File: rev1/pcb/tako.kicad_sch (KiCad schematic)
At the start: 118 parts, among them J1 MJ-4PP-9, J101 MJ-4PP-9, SW1 EC_SW, SW10 EC_SW, SW101 EC_SW, SW102 EC_SW, SW103 EC_SW, SW104 EC_SW, SW105 EC_SW, SW106 EC_SW, SW107 EC_SW, SW108 EC_SW, SW109 EC_SW, SW11 EC_SW, SW110 EC_SW, SW111 EC_SW, SW112 EC_SW, SW113 EC_SW, SW114 EC_SW, SW115 EC_SW, SW116 EC_SW, SW117 EC_SW, SW12 EC_SW, SW13 EC_SW, SW14 EC_SW, SW15 EC_SW, SW16 EC_SW, SW17 EC_SW, SW2 EC_SW, SW3 EC_SW, SW4 EC_SW, SW5 EC_SW, SW6 EC_SW, SW7 EC_SW, SW8 EC_SW, SW9 EC_SW, U1 STeMCell, U101 STeMCell, U102 74HC4051, U103 OPA350, U2 74HC4051, U3 OPA350

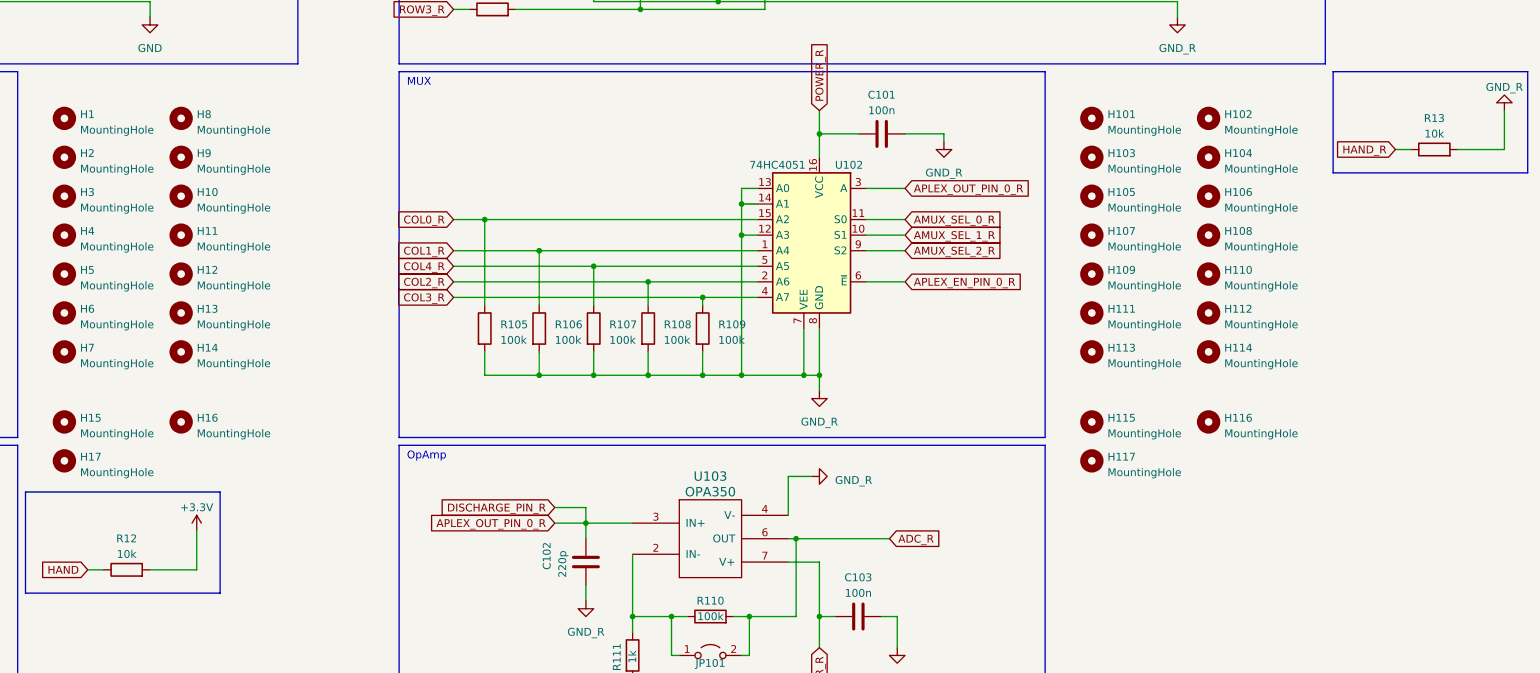
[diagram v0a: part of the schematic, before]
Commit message: Add build guide components section
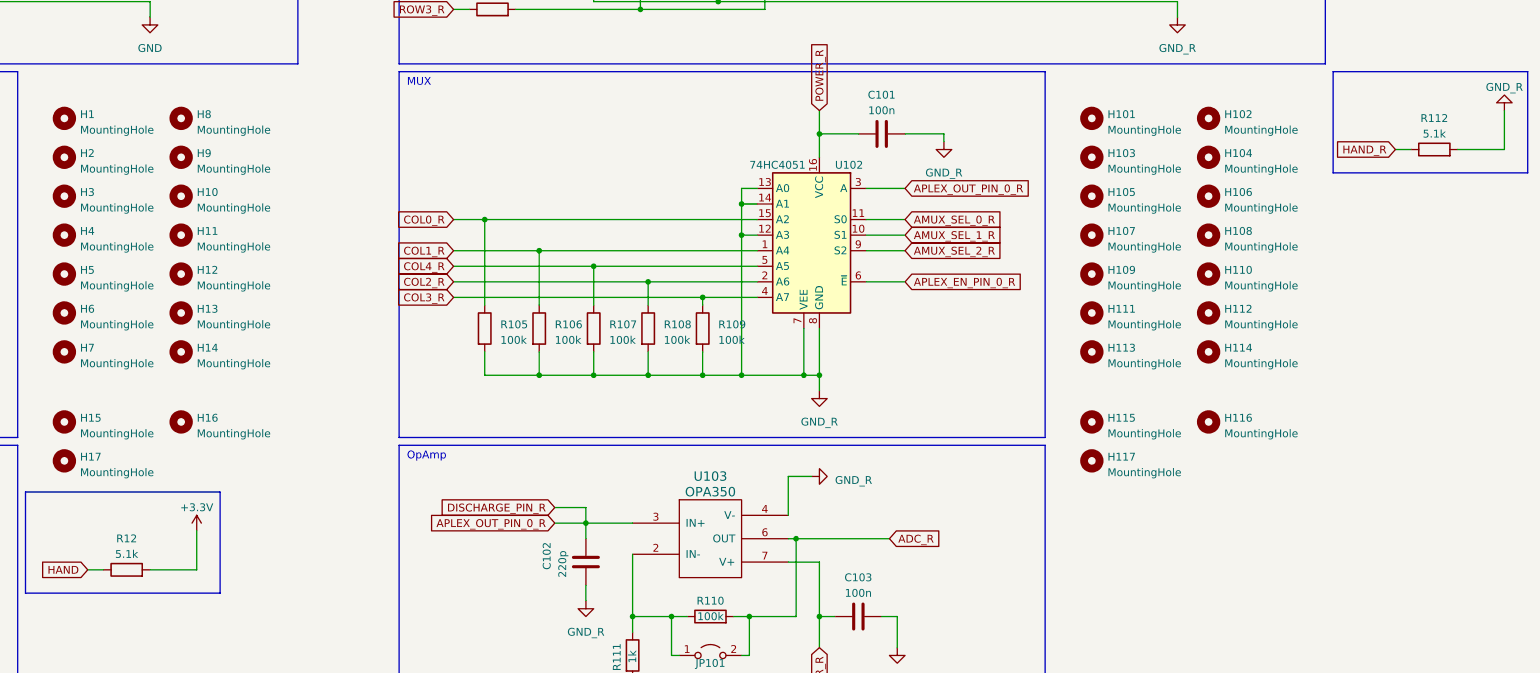
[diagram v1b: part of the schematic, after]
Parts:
- R112: renamed from R13; value 10k -> 5.1k
- R12: value 10k -> 5.1k
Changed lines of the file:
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@@
   (symbol (lib_id "Device:R") (at 350.52 189.23 90) (unit 1)
     (in_bom yes) (on_board yes) (dnp no) (fields_autoplaced)
-    (property "Reference" "R13" (at 350.52 184.15 90)
-      (effects (font (size 1.27 1.27)))
-    )
-    (property "Value" "10k" (at 350.52 186.69 90)
+    (property "Reference" "R112" (at 350.52 184.15 90)
+      (effects (font (size 1.27 1.27)))
+    )
+    (property "Value" "5.1k" (at 350.52 186.69 90)
       (effects (font (size 1.27 1.27)))
     )
@@
       (project "tako"
         (path "/72340b64-d7ab-445f-b1ce-2d9b5de13513"
-          (reference "R13") (unit 1)
+          (reference "R112") (unit 1)
         )
       )
@@
       (effects (font (size 1.27 1.27)))
     )
-    (property "Value" "10k" (at 137.16 255.27 90)
-      (effects (font (size 1.27 1.27)))
-    )
+    (property "Value" "5.1k" (at 137.16 255.27 90)
+      (effects (font (size 1.27 1.27)))
+    )

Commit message: updated code for 36key
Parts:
- added H18, H19: MountingHole, tako:MountingHole_3.4mm, symbol Mechanical:MountingHole
- added SW118, SW18: EC_SW, tako:ecs_pad_1U_no_ring_90deg, symbol tako:EC_SW
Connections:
- net COL2: now also SW18.1
- net COL2_R: now also SW118.1
- net GND: now also SW18.3 (SG)
- net GND_R: now also SW118.3 (SG)
- net at R4.2, SW16.2, SW17.2: now also SW18.2
- net at R104.2, SW116.2, SW117.2: now also SW118.2
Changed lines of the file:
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@@
   (junction (at 69.85 226.06) (diameter 0) (color 0 0 0 0)
   )
+  (junction (at 245.11 140.97) (diameter 0) (color 0 0 0 0)
+  )
   (junction (at 36.83 200.66) (diameter 0) (color 0 0 0 0)
   )
@@
   (junction (at 219.71 265.43) (diameter 0) (color 0 0 0 0)
   )
+  (junction (at 73.66 166.37) (diameter 0) (color 0 0 0 0)
+  )
   (junction (at 58.42 265.43) (diameter 0) (color 0 0 0 0)
   )
@@
   (junction (at 66.04 111.76) (diameter 0) (color 0 0 0 0)
   )
+  (junction (at 86.36 165.1) (diameter 0) (color 0 0 0 0)
+  )
   (junction (at 261.62 148.59) (diameter 0) (color 0 0 0 0)
   )
@@
   (junction (at 274.32 129.54) (diameter 0) (color 0 0 0 0)
   )
+  (junction (at 77.47 140.97) (diameter 0) (color 0 0 0 0)
+  )
   (junction (at 86.36 129.54) (diameter 0) (color 0 0 0 0)
   )
@@
   (junction (at 245.11 105.41) (diameter 0) (color 0 0 0 0)
   )
+  (junction (at 254 165.1) (diameter 0) (color 0 0 0 0)
+  )
   (junction (at 237.49 226.06) (diameter 0) (color 0 0 0 0)
   )
@@
   (junction (at 86.36 147.32) (diameter 0) (color 0 0 0 0)
   )
+  (junction (at 241.3 166.37) (diameter 0) (color 0 0 0 0)
+  )
   (junction (at 254 111.76) (diameter 0) (color 0 0 0 0)
   )
@@
     (stroke (width 0) (type default))
   )
+  (wire (pts (xy 245.11 160.02) (xy 246.38 160.02))
+    (stroke (width 0) (type default))
+  )
   (wire (pts (xy 52.07 265.43) (xy 52.07 267.97))
     (stroke (width 0) (type default))
@@
     (stroke (width 0) (type default))
   )
+  (wire (pts (xy 77.47 140.97) (xy 77.47 160.02))
+    (stroke (width 0) (type default))
+  )
   (wire (pts (xy 119.38 29.21) (xy 119.38 21.59))
     (stroke (width 0) (type default))
@@
     (stroke (width 0) (type default))
   )
+  (wire (pts (xy 94.107 160.02) (xy 94.107 166.37))
+    (stroke (width 0) (type default))
+  )
   (wire (pts (xy 262.89 113.03) (xy 283.21 113.03))
     (stroke (width 0) (type default))
@@
     (stroke (width 0) (type default))
   )
-  (wire (pts (xy 233.68 165.1) (xy 308.61 165.1))
+  (wire (pts (xy 254 165.1) (xy 308.61 165.1))
+    (stroke (width 0) (type default))
+  )
+  (wire (pts (xy 233.68 165.1) (xy 254 165.1))
     (stroke (width 0) (type default))
   )
@@
     (stroke (width 0) (type default))
   )
+  (wire (pts (xy 86.36 165.1) (xy 140.97 165.1))
+    (stroke (width 0) (type default))
+  )
   (wire (pts (xy 254 110.49) (xy 254 111.76))
     (stroke (width 0) (type default))
@@
     (stroke (width 0) (type default))
   )
+  (wire (pts (xy 94.107 166.37) (xy 73.66 166.37))
+    (stroke (width 0) (type default))
+  )
   (wire (pts (xy 33.02 53.34) (xy 35.56 53.34))
     (stroke (width 0) (type default))
@@
     (stroke (width 0) (type default))
   )
+  (wire (pts (xy 93.98 160.02) (xy 94.107 160.02))
+    (stroke (width 0) (type default))
+  )
   (wire (pts (xy 245.11 105.41) (xy 245.11 123.19))
     (stroke (width 0) (type default))
@@
     (stroke (width 0) (type default))
   )
+  (wire (pts (xy 77.47 160.02) (xy 78.74 160.02))
+    (stroke (width 0) (type default))
+  )
   (wire (pts (xy 281.94 140.97) (xy 281.94 148.59))
     (stroke (width 0) (type default))
@@
     (stroke (width 0) (type default))
   )
+  (wire (pts (xy 245.11 140.97) (xy 245.11 160.02))
+    (stroke (width 0) (type default))
+  )
   (wire (pts (xy 274.32 111.76) (xy 294.64 111.76))
     (stroke (width 0) (type default))
@@
     (stroke (width 0) (type default))
   )
-  (wire (pts (xy 66.04 165.1) (xy 140.97 165.1))
+  (wire (pts (xy 66.04 165.1) (xy 86.36 165.1))
     (stroke (width 0) (type default))
   )
@@
     (stroke (width 0) (type default))
   )
+  (wire (pts (xy 241.3 166.37) (xy 261.62 166.37))
+    (stroke (width 0) (type default))
+  )
   (wire (pts (xy 73.66 123.19) (xy 73.66 130.81))
     (stroke (width 0) (type default))
@@
     (stroke (width 0) (type default))
   )
+  (wire (pts (xy 261.62 166.37) (xy 261.62 160.02))
+    (stroke (width 0) (type default))
+  )
   (wire (pts (xy 33.02 40.64) (xy 35.56 40.64))
     (stroke (width 0) (type default))
@@
     )
   )
+  (symbol (lib_id "Mechanical:MountingHole") (at 164.465 217.043 0) (unit 1)
+    (in_bom yes) (on_board yes) (dnp no) (fields_autoplaced)
+    (property "Reference" "H19" (at 167.005 216.408 0)
+      (effects (font (size 1.27 1.27)) (justify left))
+    )
+    (property "Value" "MountingHole" (at 167.005 218.948 0)
+      (effects (font (size 1.27 1.27)) (justify left))
+    )
+    (property "Footprint" "tako:MountingHole_3.4mm" (at 164.465 217.043 0)
+      (effects (font (size 1.27 1.27)) hide)
+    )
+    (property "Datasheet" "~" (at 164.465 217.043 0)
+      (effects (font (size 1.27 1.27)) hide)
+    )
+    (instances
+      (project "tako"
+        (path "/72340b64-d7ab-445f-b1ce-2d9b5de13513"
+          (reference "H19") (unit 1)
+        )
+      )
+    )
+  )
   (symbol (lib_id "Mechanical:MountingHole_Pad") (at 95.25 63.5 0) (unit 1)
     (in_bom yes) (on_board yes) (dnp no) (fields_autoplaced)
@@
     )
   )
+  (symbol (lib_id "tako:EC_SW") (at 86.36 160.02 0) (unit 1)
+    (in_bom yes) (on_board yes) (dnp no) (fields_autoplaced)
+    (property "Reference" "SW18" (at 86.36 153.67 0)
+      (effects (font (size 1.27 1.27)))
+    )
+    (property "Value" "EC_SW" (at 86.36 156.21 0)
+      (effects (font (size 1.27 1.27)))
+    )
+    (property "Footprint" "tako:ecs_pad_1U_no_ring_90deg" (at 86.36 160.02 0)
+      (effects (font (size 1.27 1.27)) hide)
+    )
+    (property "Datasheet" "" (at 86.36 160.02 0)
+      (effects (font (size 1.27 1.27)))
+    )
+    (pin "1")
+    (pin "2")
+    (pin "3")
+    (instances
+      (project "tako"
+        (path "/72340b64-d7ab-445f-b1ce-2d9b5de13513"
+          (reference "SW18") (unit 1)
+        )
+      )
+    )
+  )
   (symbol (lib_id "tako:GND_R") (at 262.89 270.51 0) (unit 1)
     (in_bom yes) (on_board yes) (dnp no) (fields_autoplaced)
@@
     )
   )
+  (symbol (lib_id "tako:EC_SW") (at 254 160.02 0) (unit 1)
+    (in_bom yes) (on_board yes) (dnp no) (fields_autoplaced)
+    (property "Reference" "SW118" (at 254 152.4 0)
+      (effects (font (size 1.27 1.27)))
+    )
+    (property "Value" "EC_SW" (at 254 154.94 0)
+      (effects (font (size 1.27 1.27)))
+    )
+    (property "Footprint" "tako:ecs_pad_1U_no_ring_90deg" (at 254 160.02 0)
+      (effects (font (size 1.27 1.27)) hide)
+    )
+    (property "Datasheet" "" (at 254 160.02 0)
+      (effects (font (size 1.27 1.27)))
+    )
+    (pin "1")
+    (pin "2")
+    (pin "3")
+    (instances
+      (project "tako"
+        (path "/72340b64-d7ab-445f-b1ce-2d9b5de13513"
+          (reference "SW118") (unit 1)
+        )
+      )
+    )
+  )
   (symbol (lib_id "tako:EC_SW") (at 254 123.19 0) (unit 1)
     (in_bom yes) (on_board yes) (dnp no) (fields_autoplaced)
@@
         )
       )
+    )
+  )
+  (symbol (lib_id "Mechanical:MountingHole") (at 164.592 224.155 0) (unit 1)
+    (in_bom yes) (on_board yes) (dnp no) (fields_autoplaced)
+    (property "Reference" "H18" (at 167.132 223.52 0)
+      (effects (font (size 1.27 1.27)) (justify left))
+    )
+    (property "Value" "MountingHole" (at 167.132 226.06 0)
+      (effects (font (size 1.27 1.27)) (justify left))
+    )
+    (property "Footprint" "tako:MountingHole_3.4mm" (at 164.592 224.155 0)
+      (effects (font (size 1.27 1.27)) hide)
+    )
+    (property "Datasheet" "~" (at 164.592 224.155 0)
+      (effects (font (size 1.27 1.27)) hide)
+    )
+    (instances
+      (project "tako"
+        (path "/72340b64-d7ab-445f-b1ce-2d9b5de13513"
+          (reference "H18") (unit 1)
+        )
+      )
